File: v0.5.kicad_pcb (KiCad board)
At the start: 2 copper layers, 82 x 38 mm, 61 parts, among them J1 USB_B_Micro, J2 Conn_02x06_Odd_Even, J3 Screw_Terminal_01x08, J4 Screw_Terminal_01x04, J5 Conn_Coaxial_Small, Q1 MMBT3904, Q2 SiS454DN, Q3 SiS454DN, Q4 SiS454DN, Q5 SiS454DN, U1 MS5611-01BA, U2 L7805, U3 ACS711xLCTR-25AB, U4 ICM-42670-P, U5 SAM-M10Q-0-10, U6 ADXL375BCCZ, U7 Teensy4.1, U8 RFM69W

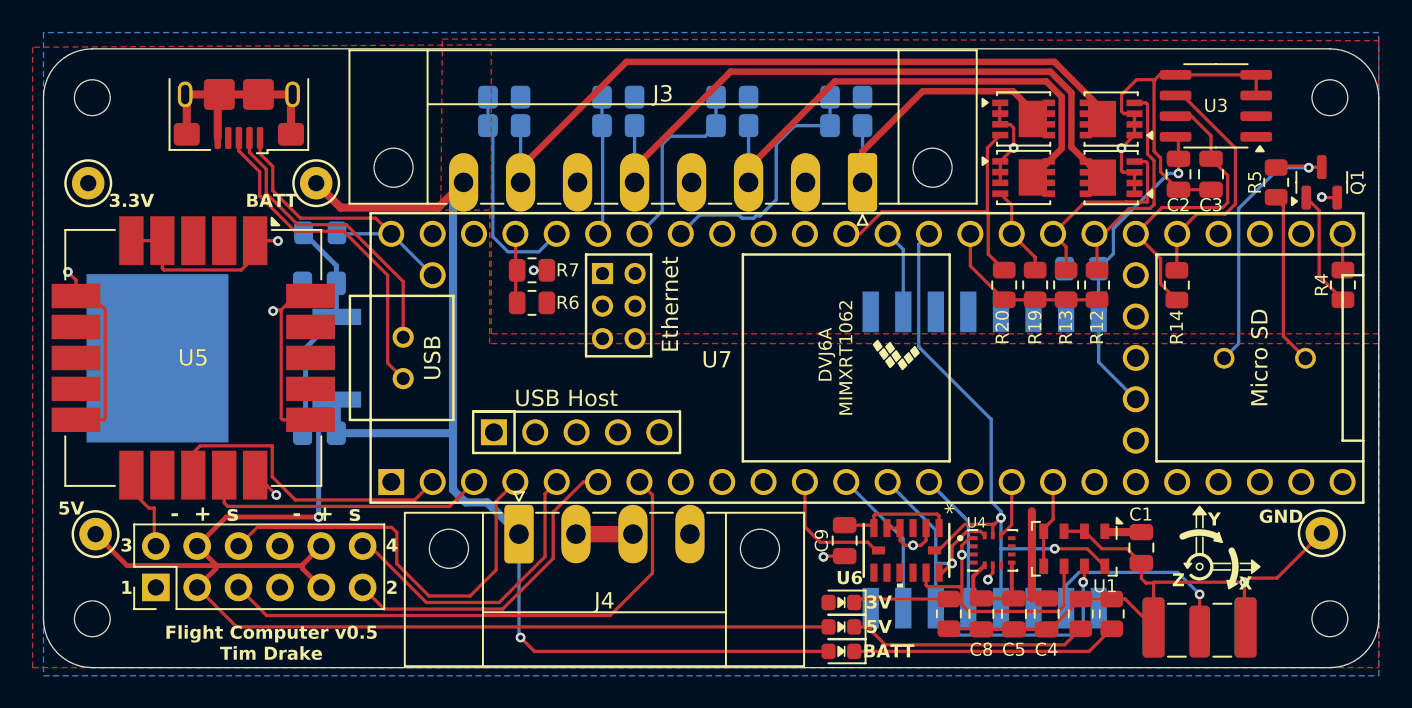
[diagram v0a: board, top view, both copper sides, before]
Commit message: Added test pin headers. Updated BOM
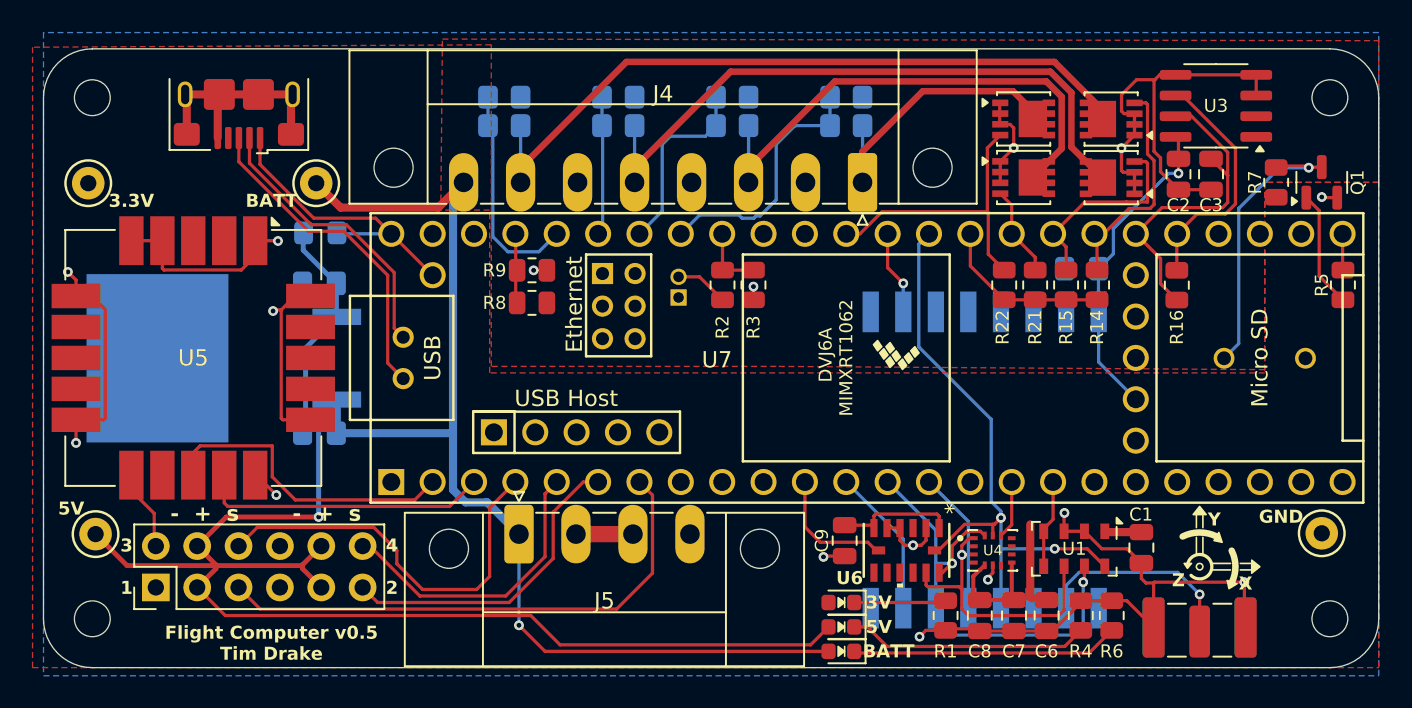
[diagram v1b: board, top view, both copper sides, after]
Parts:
- added J1: Conn_01x02_Pin, Connector_PinHeader_1.27mm:PinHeader_1x02_P1.27mm_Horizontal, B.Cu at (122.7, 89.7)
- added R2: 270, Resistor_SMD:R_0805_2012Metric, F.Cu at (125.4, 88.9)
- added R3: 91, Resistor_SMD:R_0805_2012Metric, F.Cu at (127.3, 88.9)
- moved R1 0.22 mm to (139.1, 109.2)
- moved C8 0.14 mm to (141.2, 109.2)
- moved C6 0.10 mm to (145.3, 109.2)
- moved C7 0.10 mm to (143.3, 109.2)
- moved R4 0.10 mm to (147.4, 109.2)
- moved R6 0.10 mm to (149.3, 109.2)
- renumbered C6 to C4, C7 to C5, C4 to C6, C5 to C7, J1 to J2, J2 to J3, J3 to J4, J4 to J5, J5 to J6, R8 to R10, R9 to R11, R10 to R12, R11 to R13, R12 to R14, R13 to R15, R14 to R16, R15 to R17, R16 to R18, R17 to R19, R18 to R20, R19 to R21, R20 to R22, R2 to R4, R4 to R5, R3 to R6, R5 to R7, R6 to R8, R7 to R9
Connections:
- J2 pad 4: unconnected-(J1-ID-Pad4) -> (no net)
- J5 pad 2: Net-(J4-Pin_2) -> (no net)
- J5 pad 3: Net-(J4-Pin_2) -> (no net)
- U7 pad 40: unconnected-(U7-18_A4_SDA-Pad40) -> /TEST_MODE
- U7 pad 60: /ETH_R+ -> unconnected-(U7-R+-Pad60)
- U7 pad 61: /ETH_LED -> unconnected-(U7-LED-Pad61)
- U7 pad 62: /ETH_T- -> unconnected-(U7-T--Pad62)
- U7 pad 63: /ETH_T+ -> unconnected-(U7-T+-Pad63)
- U7 pad 65: /ETH_R- -> unconnected-(U7-R--Pad65)
- U8 pad 1: /RST -> unconnected-(U8-RESET-Pad1)
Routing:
- net +3.3V: track 53.6 -> 42.1 mm
- net /TEST_MODE: track 0.00 -> 4.11 mm
- net Net-(J5-Pin_2): track 0.00 -> 3.50 mm
- net Net-(J4-Pin_2): track 3.50 -> 0.00 mm
- net Net-(J1-Pin_2): track 0.00 -> 3.29 mm
- net /C_MEAS: track 18.7 -> 20.2 mm
- net GND: track 143.2 -> 142.0 mm, vias 12 -> 16
- net /SERVO_3: track 25.7 -> 24.7 mm
- net /MISO: track 25.4 -> 26.3 mm
- net +5V: track 88.0 -> 88.9 mm
- net / INTRPT: vias 0 -> 1
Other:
- board text added: "M2"
- board text added: "TEST MODE"

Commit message: Using RFM95W radio now instead of RFM69W.
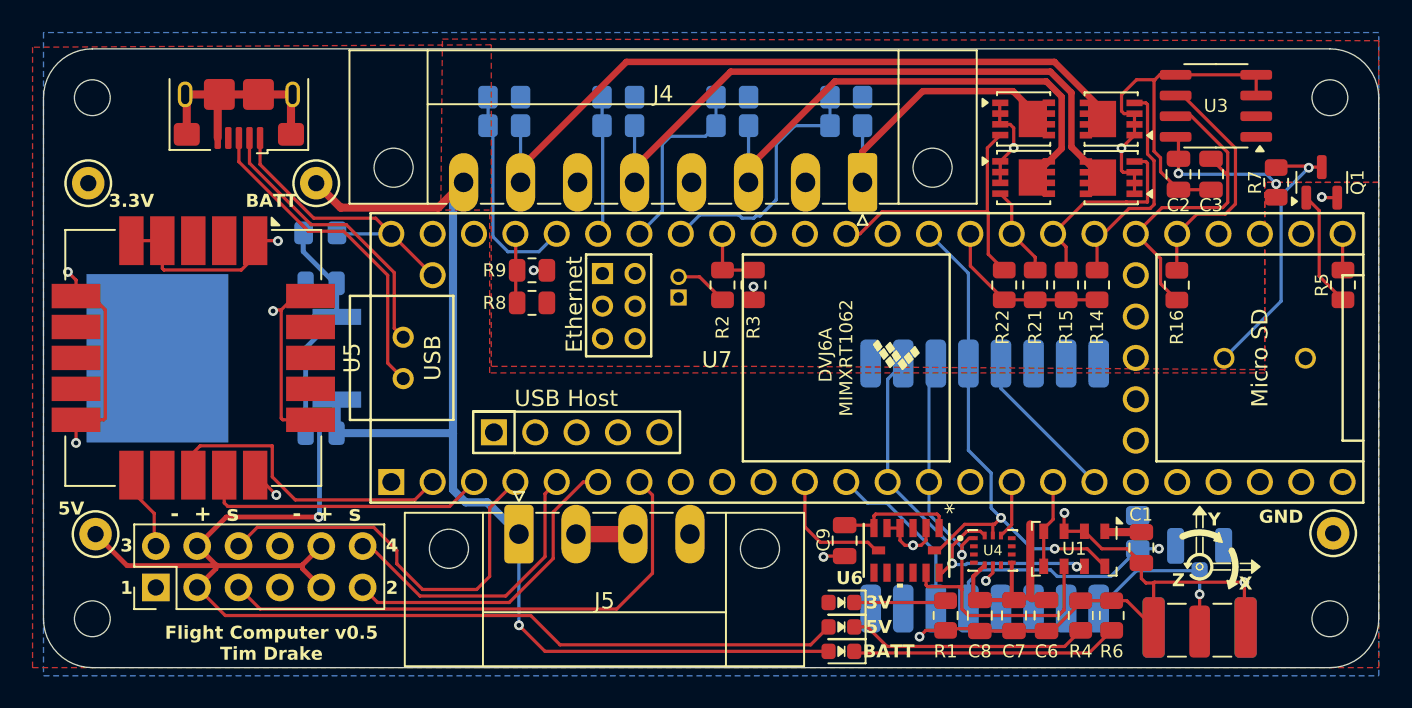
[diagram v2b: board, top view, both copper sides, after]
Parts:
- added J6: Conn_Coaxial_Small, Connector_Coaxial:U.FL_Hirose_U.FL-R-SMT-1_Vertical, B.Cu at (154.7, 105.4)
- C4, C5: footprint Capacitor_SMD:C_0805_2012Metric_Pad1.18x1.45mm_HandSolder -> Capacitor_SMD:C_0805_2012Metric
- C9: value 10U -> 1u
- U8: value RFM69W -> RFM95W-868S2; footprint RF_Module:HOPERF_RFM69HW -> RF_Module:HOPERF_RFM9XW_SMD
- moved C10 16.6 mm to (150.9, 104.1), turned to 90 degrees
- moved U8 1.60 mm to (141.5, 101.2)
- moved TP4 0.70 mm to (162.9, 104.2)
- moved C4 0.10 mm to (100.8, 98.0)
- moved C5 0.10 mm to (100.8, 88.8)
- turned C9 to -90 degrees
- renumbered J6 to J7
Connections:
- C9 pad 1: GND -> +3.3V
- C9 pad 2: +3.3V -> GND
- J1 pad 2: (no net) -> Net-(J1-Pin_2)
- J2 pad 4: (no net) -> unconnected-(J2-ID-Pad4)
- J5 pad 2: (no net) -> Net-(J5-Pin_2)
- J5 pad 3: (no net) -> Net-(J5-Pin_2)
- U7 pad 12: /CS_RADIO -> /INTRPT
- U7 pad 18: unconnected-(U7-26_A12_MOSI1-Pad18) -> /CS_RADIO
- U7 pad 36: / INTRPT -> unconnected-(U7-14_A0_TX3_SPDIF_OUT-Pad36)
- U8 pad 1: unconnected-(U8-RESET-Pad1) -> GND
- U8 pad 10: /ANT -> GND
- U8 pad 11: GND -> unconnected-(U8-DIO3-Pad11)
- U8 pad 12: /SCK -> unconnected-(U8-DIO4-Pad12)
- U8 pad 13: /MISO -> +3.3V
- U8 pad 14: /MOSI -> /INTRPT
- U8 pad 15: /CS_RADIO -> unconnected-(U8-DIO1-Pad15)
- U8 pad 2: / INTRPT -> /MOSI
- U8 pad 3: unconnected-(U8-DIO1-Pad3) -> /MISO
- U8 pad 4: unconnected-(U8-DIO2-Pad4) -> /SCK
- U8 pad 5: unconnected-(U8-DIO3-Pad5) -> /CS_RADIO
- U8 pad 8: +3.3V -> GND
- U8 pad 9: GND -> /ANT
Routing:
- net /INTRPT: track 0.00 -> 10.8 mm
- net /SCK: track 37.5 -> 32.2 mm
- net / INTRPT: track 5.19 -> 0.00 mm, vias 1 -> 0
- net +3.3V: track 42.1 -> 46.5 mm, vias 1 -> 3
- net /MISO: track 26.3 -> 29.5 mm
- net GND: track 142.0 -> 145.1 mm
- net /ANT: track 12.8 -> 10.9 mm
- net Net-(Q1-C): track 17.8 -> 16.7 mm
- net /MOSI: track 28.0 -> 27.2 mm

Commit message: Ready to buy
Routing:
- net GND: track 145.1 -> 149.8 mm
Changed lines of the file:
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@@
 	)
 	(segment
-		(start 146.5 107.35)
-		(end 146.5 108.75)
+		(start 141.7 106.8)
+		(end 144.873278 106.8)
 		(width 0.2)
 		(layer "B.Cu")
+		(net 71)
+	)
+	(segment
+		(start 141.572549 107.07133)
+		(end 141.572549 106.927451)
+		(width 0.2)
+		(layer "B.Cu")
+		(net 71)
+	)
+	(segment
+		(start 146.5 108.426722)
+		(end 146.5 108.775)
+		(width 0.2)
+		(layer "B.Cu")
+		(net 71)
+	)
+	(segment
+		(start 141.572549 106.927451)
+		(end 141.7 106.8)
+		(width 0.2)
+		(layer "B.Cu")
+		(net 71)
+	)
+	(segment
+		(start 144.873278 106.8)
+		(end 146.5 108.426722)
+		(width 0.2)
+		(layer "B.Cu")
